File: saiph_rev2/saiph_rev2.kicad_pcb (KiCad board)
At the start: 2 copper layers, 347.7 x 126.6 mm, 206 parts, among them M1 MISC, SW1 SW_PUSH, SW10 SW_PUSH, SW100 SW_PUSH, SW101 SW_PUSH, SW102 SW_PUSH, SW103 SW_PUSH, SW104 SW_PUSH, SW105 SW_PUSH, SW109 SW_PUSH, SW11 SW_PUSH, SW110 SW_PUSH, SW111 SW_PUSH, SW12 SW_PUSH, SW13 SW_PUSH, SW14 SW_PUSH, SW15 SW_PUSH, SW16 SW_PUSH, SW17 SW_PUSH, SW18 SW_PUSH, SW19 SW_PUSH, SW2 SW_PUSH, SW20 SW_PUSH, SW21 SW_PUSH, SW22 SW_PUSH, SW23 SW_PUSH, SW24 SW_PUSH, SW25 SW_PUSH, SW26 SW_PUSH, SW27 SW_PUSH, SW28 SW_PUSH, SW29 SW_PUSH, SW3 SW_PUSH, SW30 SW_PUSH, SW31 SW_PUSH, SW32 SW_PUSH, SW33 SW_PUSH, SW34 SW_PUSH, SW35 SW_PUSH, SW36 SW_PUSH, SW37 SW_PUSH, SW38 SW_PUSH, SW39 SW_PUSH, SW4 SW_PUSH, SW40 SW_PUSH, SW41 SW_PUSH, SW42 SW_PUSH, SW43 SW_PUSH, SW44 SW_PUSH, SW45 SW_PUSH, SW46 SW_PUSH, SW47 SW_PUSH, SW48 SW_PUSH, SW49 SW_PUSH, SW5 SW_PUSH, SW50 SW_PUSH, SW51 SW_PUSH, SW52 SW_PUSH, SW53 SW_PUSH, SW54 SW_PUSH, SW55 SW_PUSH, SW56 SW_PUSH, SW57 SW_PUSH, SW58 SW_PUSH, SW59 SW_PUSH, SW6 SW_PUSH, SW60 SW_PUSH, SW61 SW_PUSH, SW62 SW_PUSH, SW63 SW_PUSH, SW64 SW_PUSH, SW65 SW_PUSH, SW66 SW_PUSH, SW67 SW_PUSH, SW68 SW_PUSH, SW69 SW_PUSH, SW7 SW_PUSH, SW70 SW_PUSH, SW71 SW_PUSH, SW72 SW_PUSH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

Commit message: add pro micro and usb
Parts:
- added J1: USB_mini_micro_B, keyboard_parts:USB_miniB_hirose_5S8, F.Cu at (278.6, -10.9)
- added U1: ProMicro, promicro:ProMicro, B.Cu at (81.0, 100.0)
- moved D37 39.0 mm to (61.9, 97.5), turned to -90 degrees
- moved D32 28.1 mm to (109.5, 85.7), turned to 90 degrees
- moved D22 10.5 mm to (33.3, 90.4)
- moved D27 10.3 mm to (52.4, 90.5)
- moved D16 7.23 mm to (23.8, 85.7)
- moved D15 5.71 mm to (23.8, 71.3)
- moved D10 2.26 mm to (23.8, 76.2)
- moved D11 1.79 mm to (23.7, 81.0)

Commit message: add promicro
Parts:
- added J2: Conn_01x04, Connector_PinHeader_2.54mm:PinHeader_1x04_P2.54mm_Vertical, F.Cu at (109.0, 96.2)
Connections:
- U1 pad 10: unconnected-(U1-Pad10) -> /C2
- U1 pad 11: unconnected-(U1-Pad11) -> /C1
- U1 pad 12: unconnected-(U1-Pad12) -> /C0
- U1 pad 13: unconnected-(U1-Pad13) -> /R0
- U1 pad 14: unconnected-(U1-Pad14) -> /R1
- U1 pad 15: unconnected-(U1-Pad15) -> /R2
- U1 pad 16: unconnected-(U1-Pad16) -> /R3
- U1 pad 17: unconnected-(U1-Pad17) -> /R4
- U1 pad 18: unconnected-(U1-Pad18) -> /R5
- U1 pad 19: unconnected-(U1-Pad19) -> /C8
- U1 pad 20: unconnected-(U1-Pad20) -> /C7
- U1 pad 6: unconnected-(U1-Pad6) -> /C6
- U1 pad 7: unconnected-(U1-Pad7) -> /C5
- U1 pad 8: unconnected-(U1-Pad8) -> /C4
- U1 pad 9: unconnected-(U1-Pad9) -> /C3
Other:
- outline, holes or cut-outs redrawn

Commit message: rotate diodes
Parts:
- moved D37 44.9 mm to (105.6, 107.8), turned to 0 degrees
- moved D22 39.1 mm to (71.6, 82.5), turned to -90 degrees
- moved D27 38.0 mm to (90.4, 89.1), turned to 90 degrees
- moved D68 33.8 mm to (205.1, 103.6), turned to 90 degrees
- moved D16 29.5 mm to (52.9, 90.4), turned to 90 degrees
- moved D42 29.1 mm to (148.2, 83.5), turned to -90 degrees
- moved D52 28.6 mm to (185.8, 83.6), turned to -90 degrees
- moved D36 28.2 mm to (129.1, 91.1), turned to 90 degrees
- moved D47 28.0 mm to (167.0, 90.9), turned to 90 degrees
- moved D57 27.6 mm to (204.8, 91.1), turned to 90 degrees
- moved D6 23.0 mm to (16.2, 101.1)
- moved D61 20.0 mm to (214.8, 64.0), turned to -90 degrees
- moved D71 19.8 mm to (252.4, 44.6), turned to -90 degrees
- moved D41 19.3 mm to (138.2, 64.8), turned to -90 degrees
- moved D35 19.1 mm to (120.0, 71.3), turned to 90 degrees
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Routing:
- net /R0: track 0.00 -> 309.5 mm
- net /R1: track 0.00 -> 270.5 mm

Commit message: change footprints to attempt better fit
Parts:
- SW75, SW76, SW81, SW82: footprint keyboard_parts:ALPS_PLATE -> custom_parts:ALPS_PLATE_SPRING_PARTIAL
- moved U1 218.9 mm to (278.4, 5.62), turned to -90 degrees
- turned SW81 to 180 degrees
- turned SW82 to 180 degrees
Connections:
- U1 pad 10: /C2 -> /R4
- U1 pad 11: /C1 -> /R5
- U1 pad 12: /C0 -> /C8
- U1 pad 13: /R0 -> /C7
- U1 pad 14: /R1 -> /C6
- U1 pad 15: /R2 -> /C5
- U1 pad 16: /R3 -> /C4
- U1 pad 17: /R4 -> /C3
- U1 pad 18: /R5 -> /C2
- U1 pad 19: /C8 -> /C1
- U1 pad 20: /C7 -> /C0
- U1 pad 6: /C6 -> /R0
- U1 pad 7: /C5 -> /R1
- U1 pad 8: /C4 -> /R2
- U1 pad 9: /C3 -> /R3
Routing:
- net /R0: track 309.5 -> 266.7 mm

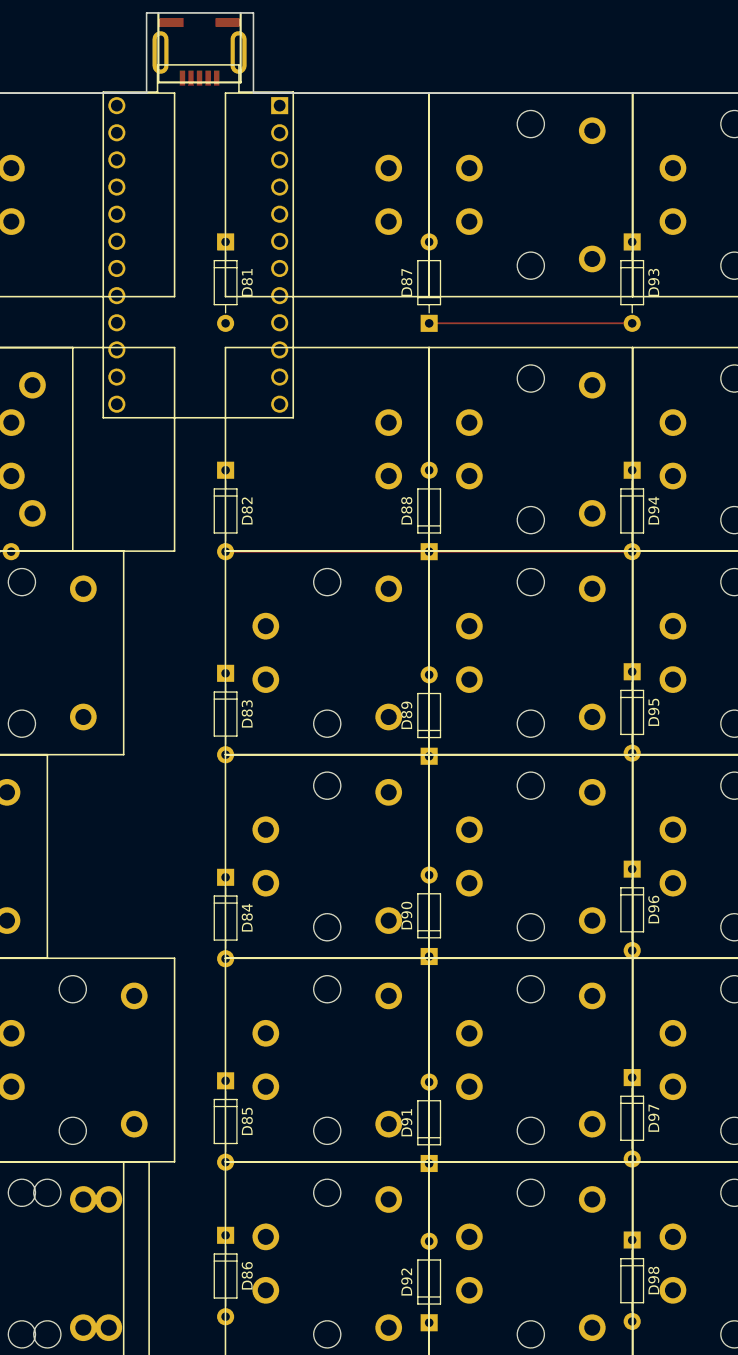
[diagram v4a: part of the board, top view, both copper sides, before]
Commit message: place rp2040 stamp and buttons; start planning routing
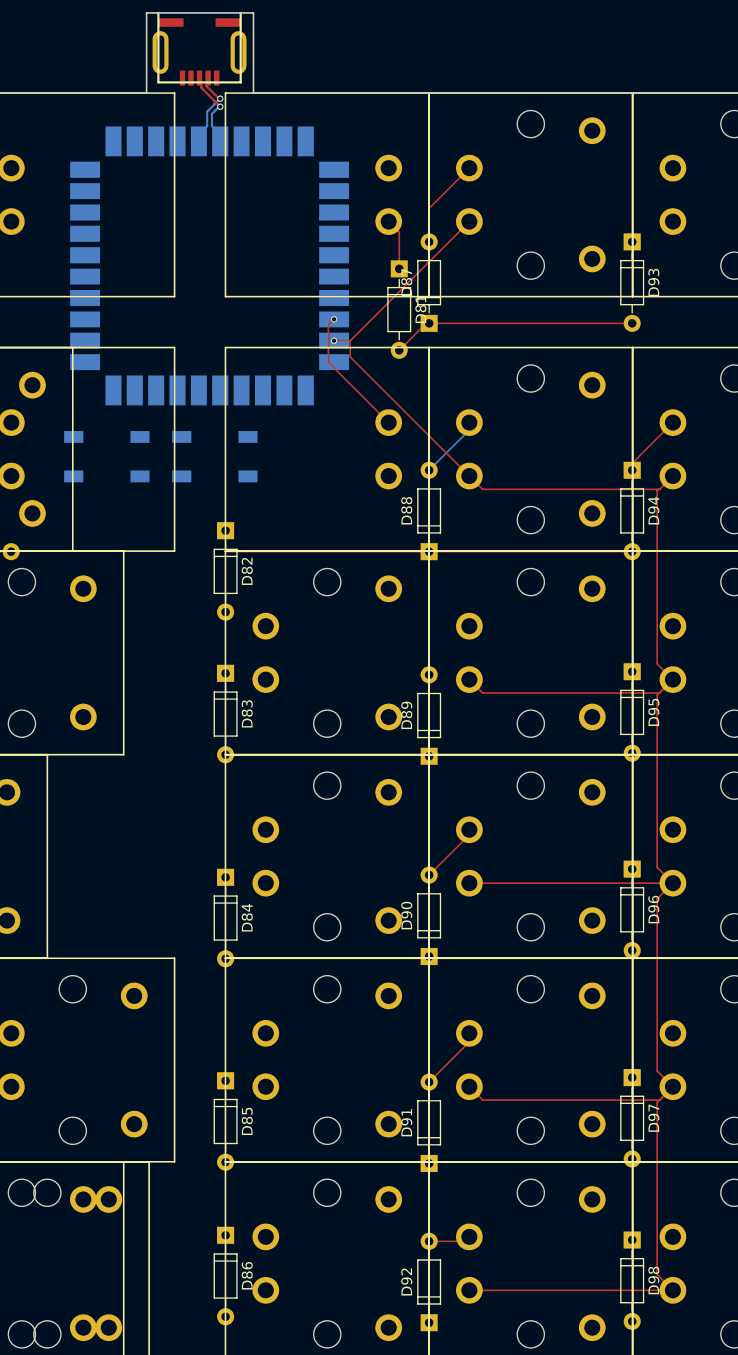
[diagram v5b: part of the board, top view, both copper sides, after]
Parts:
- added SW108: SKQGABE010, custom_parts:Switch_ALPS_SKQGABE010, B.Cu at (269.9, 24.5)
- added SW112: SKQGABE010, custom_parts:Switch_ALPS_SKQGABE010, B.Cu at (280.0, 24.5)
- U1: value ProMicro -> RP2040_Stamp; footprint promicro:ProMicro -> RP2040_Stamp:RP2040_Stamp_SMD
- moved D81 16.4 mm to (297.2, 6.92)
- moved D82 5.66 mm to (281.0, 31.4)
- moved U1 1.48 mm to (279.5, 6.65), turned to 180 degrees
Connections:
- J1 pad 1: unconnected-(J1-Pad1) -> +5V
- J1 pad 2: unconnected-(J1-Pad2) -> /USB_D-
- J1 pad 3: unconnected-(J1-Pad3) -> /USB_D+
- J1 pad 5: unconnected-(J1-Pad5) -> GND
- J1 pad 6: unconnected-(J1-Pad6) -> GND
- U1 pad 1: unconnected-(U1-Pad1) -> /C0
- U1 pad 10: /R4 -> unconnected-(U1-GPIO9-Pad10)
- U1 pad 11: /R5 -> unconnected-(U1-GPIO10-Pad11)
- U1 pad 12: /C8 -> /R0
- U1 pad 13: /C7 -> /R1
- U1 pad 14: /C6 -> /R2
- U1 pad 15: /C5 -> /R3
- U1 pad 16: /C4 -> /R4
- U1 pad 17: /C3 -> /R5
- U1 pad 18: /C2 -> unconnected-(U1-GPIO17-Pad18)
- U1 pad 19: /C1 -> unconnected-(U1-GPIO18-Pad19)
- U1 pad 2: unconnected-(U1-Pad2) -> /C1
- U1 pad 20: /C0 -> unconnected-(U1-GPIO19-Pad20)
- U1 pad 3: unconnected-(U1-Pad3) -> /C2
- U1 pad 4: unconnected-(U1-Pad4) -> /C3
- U1 pad 5: unconnected-(U1-Pad5) -> /C4
- U1 pad 6: /R0 -> /C5
- U1 pad 7: /R1 -> /C6
- U1 pad 8: /R2 -> /C7
- U1 pad 9: /R3 -> /C8
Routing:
- net /C8: track 0.00 -> 212.2 mm, vias 0 -> 1
- net /C7: track 0.00 -> 12.2 mm, vias 0 -> 1
- net Net-(D87-A): track 0.00 -> 8.46 mm
- net /USB_D-: track 0.00 -> 7.45 mm, vias 0 -> 1
- net /USB_D+: track 0.00 -> 7.45 mm, vias 0 -> 1
- net Net-(D91-A): track 0.00 -> 6.12 mm
- net Net-(D94-K): track 0.00 -> 6.04 mm
- net Net-(D88-A): track 0.00 -> 6.02 mm
- net Net-(D90-A): track 0.00 -> 5.80 mm
- net Net-(D81-K): track 0.00 -> 4.83 mm
- net Net-(D92-A): track 0.00 -> 3.93 mm
- net /R0: track 266.7 -> 270.6 mm

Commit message: remove traces.
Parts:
- moved D67 21.7 mm to (274.2, 39.1), turned to 90 degrees
- moved D6 16.2 mm to (22.7, 86.2), turned to 0 degrees
- moved D11 9.54 mm to (22.7, 89.0)
- moved D10 2.41 mm to (32.8, 82.9)
- moved D51 1.82 mm to (176.0, 63.2)
- moved D21 1.76 mm to (62.0, 63.9)
- moved D46 1.36 mm to (157.2, 70.8)
- moved D15 1.36 mm to (42.8, 71.3)
- moved D41 1.17 mm to (138.2, 63.7)
- moved D9 0.70 mm to (11.2, 71.2)
- moved D66 0.59 mm to (250.2, 91.0)
- moved D26 0.37 mm to (81.1, 71.6)
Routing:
- net /R0: track 270.6 -> 0.00 mm
- net /R1: track 270.5 -> 0.00 mm
- net /C8: track 212.2 -> 0.00 mm, vias 1 -> 0
- net /C7: track 12.2 -> 0.00 mm, vias 1 -> 0
- net Net-(D87-A): track 8.46 -> 0.00 mm
- net /USB_D-: track 7.45 -> 0.00 mm, vias 1 -> 0
- net /USB_D+: track 7.45 -> 0.00 mm, vias 1 -> 0
- net Net-(D91-A): track 6.12 -> 0.00 mm
- net Net-(D94-K): track 6.04 -> 0.00 mm
- net Net-(D88-A): track 6.02 -> 0.00 mm
- net Net-(D90-A): track 5.80 -> 0.00 mm
- net Net-(D81-K): track 4.83 -> 0.00 mm
- net Net-(D92-A): track 3.93 -> 0.00 mm

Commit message: add usb traces
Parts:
- moved U1 0.51 mm to (279.0, 6.65), turned to 0 degrees
- turned SW112 to 180 degrees
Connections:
- U1 pad 12: /R0 -> unconnected-(U1-GPIO11-Pad12)
- U1 pad 13: /R1 -> unconnected-(U1-GPIO12-Pad13)
- U1 pad 14: /R2 -> unconnected-(U1-GPIO13-Pad14)
- U1 pad 15: /R3 -> unconnected-(U1-GPIO14-Pad15)
- U1 pad 16: /R4 -> unconnected-(U1-GPIO15-Pad16)
- U1 pad 17: /R5 -> unconnected-(U1-GPIO16-Pad17)
- U1 pad 22: unconnected-(U1-GPIO21-Pad22) -> /R0
- U1 pad 23: unconnected-(U1-GPIO22-Pad23) -> /R1
- U1 pad 24: unconnected-(U1-GPIO23-Pad24) -> /R2
- U1 pad 25: unconnected-(U1-GPIO24-Pad25) -> /R3
- U1 pad 26: unconnected-(U1-GPIO25-Pad26) -> /R4
- U1 pad 27: unconnected-(U1-GPIO26-Pad27) -> /R5
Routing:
- net +5V: track 0.00 -> 30.8 mm, vias 0 -> 1
- net /USB_D+: track 0.00 -> 29.6 mm, vias 0 -> 1
- net /USB_D-: track 0.00 -> 29.6 mm, vias 0 -> 1
- net /NRST: track 0.00 -> 7.10 mm
- net /BOOTSEL: track 0.00 -> 5.59 mm

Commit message: route cols/rows; main arteries
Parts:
- moved D82 7.79 mm to (288.6, 33.2), turned to 180 degrees
- moved D67 6.16 mm to (276.2, 33.2), turned to 180 degrees
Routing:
- net /C0: track 0.00 -> 312.4 mm, vias 0 -> 1
- net /R0: track 0.00 -> 301.7 mm, vias 0 -> 1
- net /C1: track 0.00 -> 220.9 mm, vias 0 -> 1
- net /C2: track 0.00 -> 203.1 mm, vias 0 -> 1
- net /C3: track 0.00 -> 152.6 mm, vias 0 -> 1
- net /C4: track 0.00 -> 115.5 mm, vias 0 -> 1
- net /R4: track 0.00 -> 100.5 mm, vias 0 -> 1
- net /R3: track 0.00 -> 87.8 mm, vias 0 -> 1
- net /R2: track 0.00 -> 74.1 mm, vias 0 -> 1
- net /C5: track 0.00 -> 67.6 mm, vias 0 -> 1
- net /R5: track 0.00 -> 40.5 mm, vias 0 -> 1
- net /R1: track 0.00 -> 36.5 mm, vias 0 -> 1
- net /C6: track 0.00 -> 31.0 mm, vias 0 -> 1
- net Net-(D1-A): track 0.00 -> 18.1 mm
- net Net-(D93-K): track 0.00 -> 8.48 mm
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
